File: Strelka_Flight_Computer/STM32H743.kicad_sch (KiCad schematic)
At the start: 45 parts, among them J3 Conn_01x07, Q3 AO3400A, Q4 AO3400A, Q5 AO3401A, SW2 TS-1185-C-A-A-A, SW3 TS-1185-C-A-A-A, U6 STM32H743VITx, Y1 Q13FC1350000400, Y2 X1E0000210834

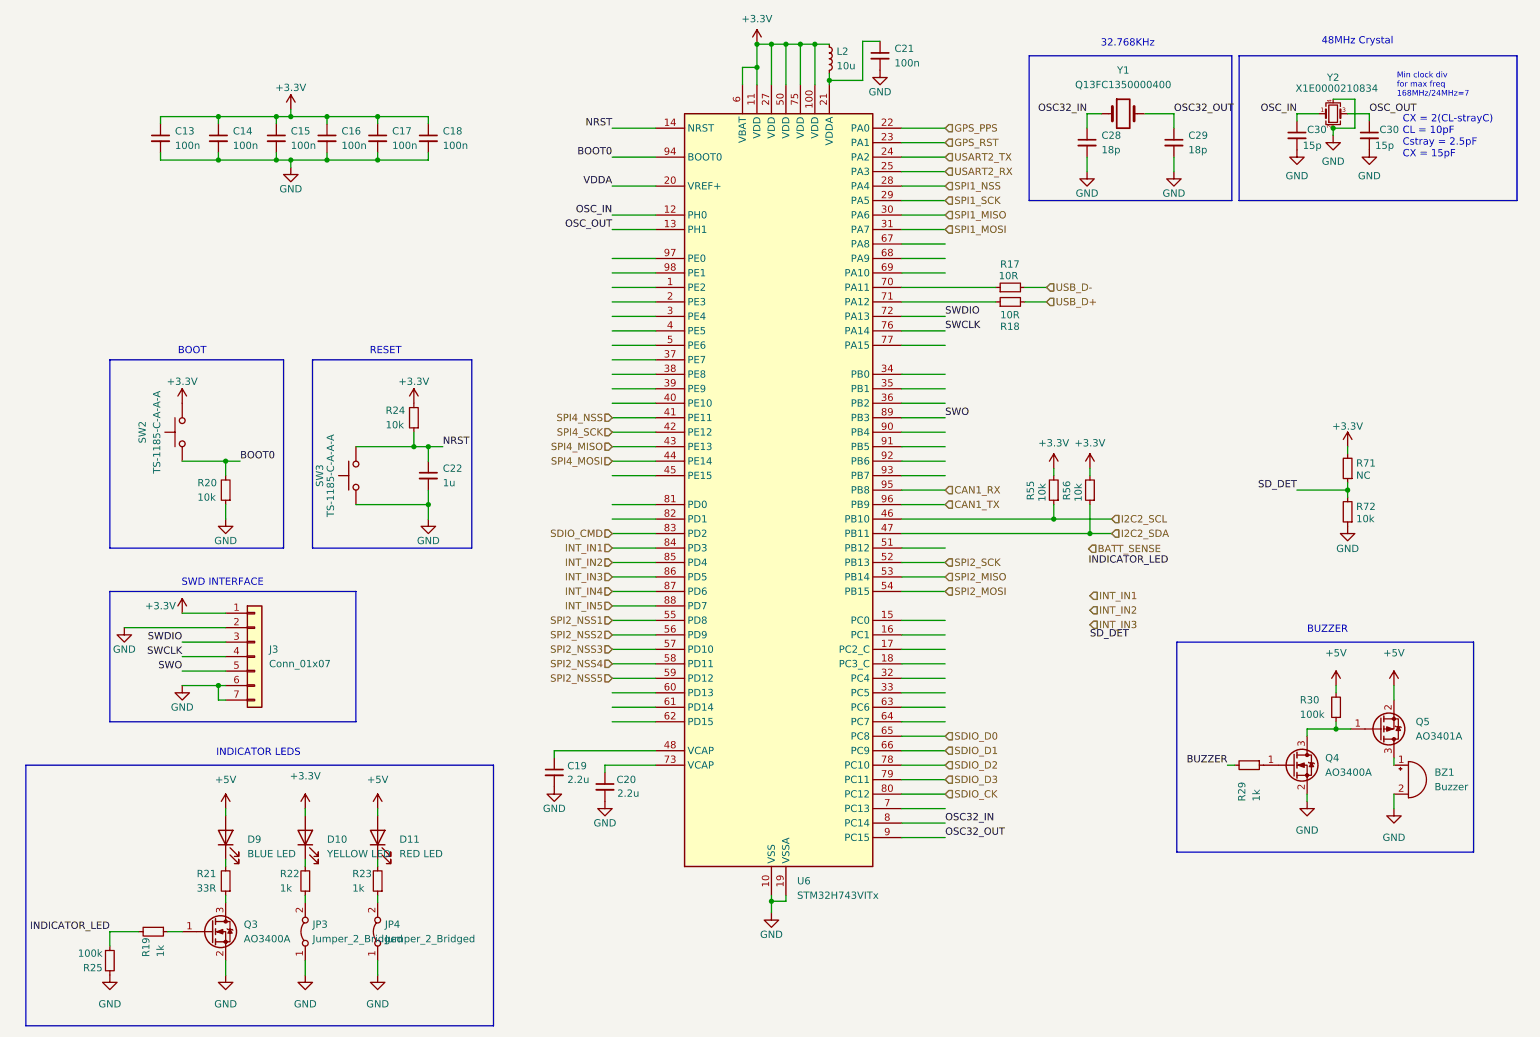
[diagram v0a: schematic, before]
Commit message: Started component placement
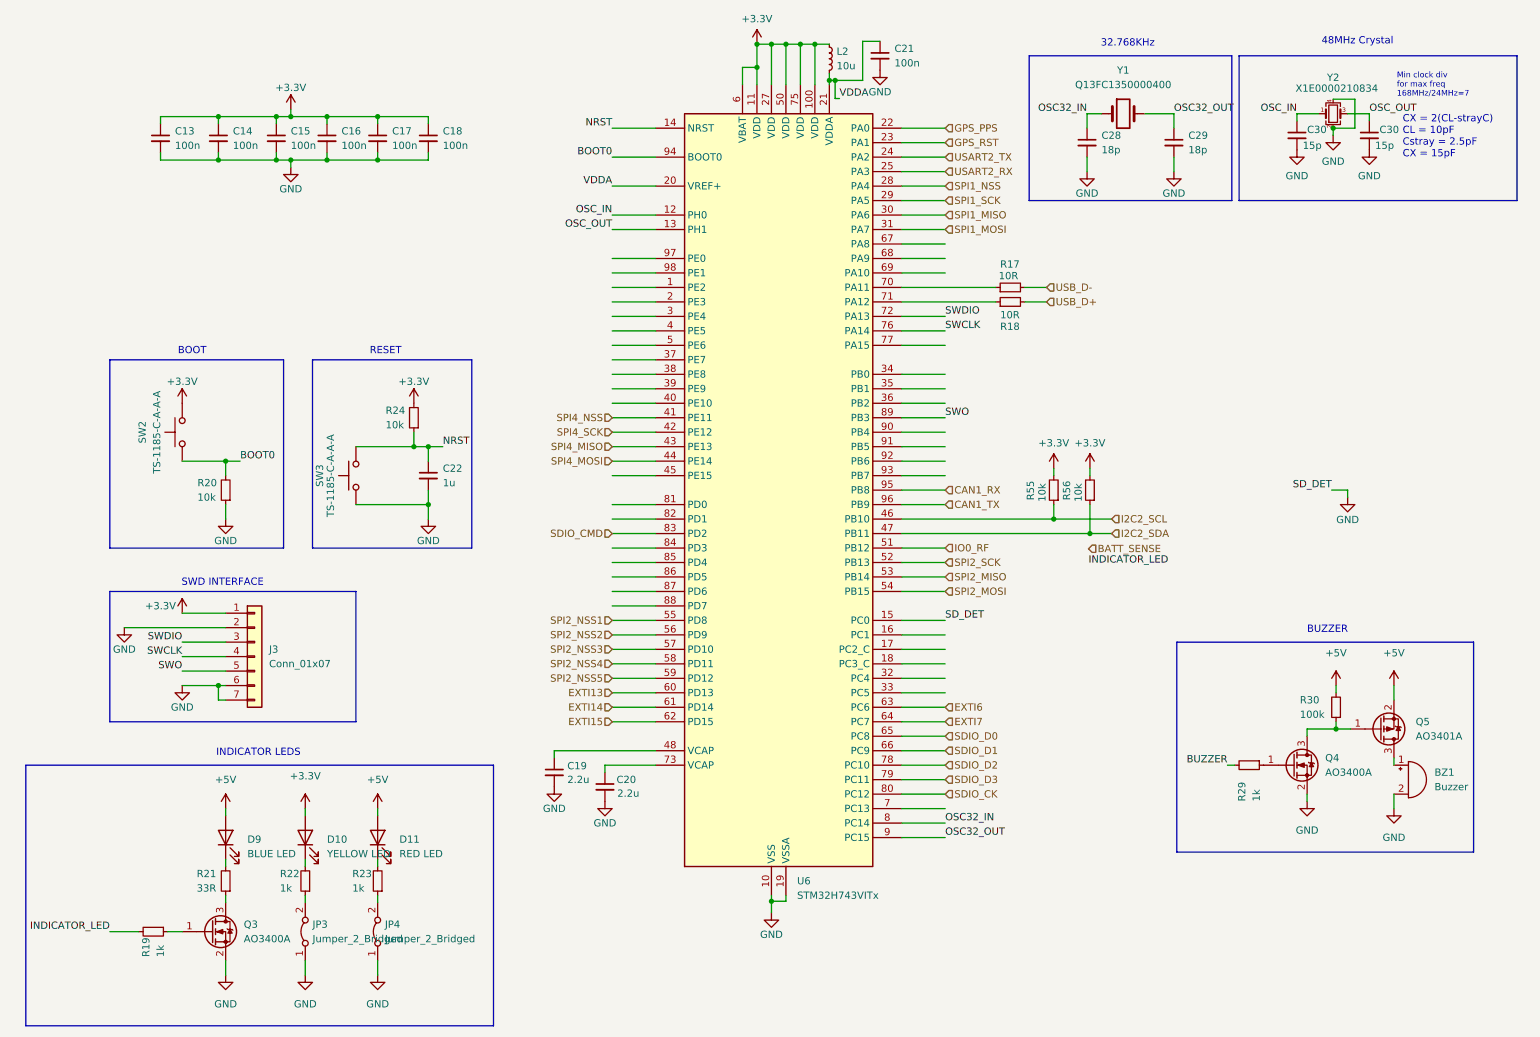
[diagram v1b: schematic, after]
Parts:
- removed R25: 100k, Resistor_SMD:R_0402_1005Metric, symbol Device:R_Small
- removed R71: NC, Resistor_SMD:R_0603_1608Metric_Pad0.98x0.95mm_HandSolder, symbol Device:R_Small
- removed R72: 10k, Resistor_SMD:R_0603_1608Metric_Pad0.98x0.95mm_HandSolder, symbol Device:R_Small
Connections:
- net GND: now also U6.15 (PC0)
- net VDDA: now also C21.1, L2.2, U6.21 (VDDA)
- net IO0_RF: now reaches U6.51 (PB12)
- net EXTI13: now reaches U6.60 (PD13)
- net EXTI14: now reaches U6.61 (PD14)
- net EXTI15: now reaches U6.62 (PD15)
- net EXTI6: now reaches U6.63 (PC6)
- net EXTI7: now reaches U6.64 (PC7)
- net INT_IN1: no longer names the net of U6.84 (PD3)
- net INT_IN2: no longer names the net of U6.85 (PD4)
- net INT_IN3: no longer names the net of U6.86 (PD5)
- net INT_IN4: no longer names the net of U6.87 (PD6)
- net INT_IN5: no longer names the net of U6.88 (PD7)

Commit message: Routing starting
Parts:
- removed R18: 10R, Resistor_SMD:R_0402_1005Metric, symbol Device:R_Small
- added R17: 10R, Resistor_SMD:R_0402_1005Metric, symbol Device:R_Small
- JP3, JP4: footprint Jumper:SolderJumper-2_P1.3mm_Bridged_Pad1.0x1.5mm -> Jumper:SolderJumper-2_P1.3mm_Bridged2Bar_RoundedPad1.0x1.5mm
- R17: LCSC (none) -> C25077
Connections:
- net USB_D+: now also R17.2
- net D-: now reaches R17.1, U6.70 (PA11)
- net D+: now reaches U6.71 (PA12)
- net D+: now also R17.1
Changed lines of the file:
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@@
     (effects (font (size 1.27 1.27)) (justify right bottom))
+  )
+  (label "D+" (at 185.674 62.992 0) (fields_autoplaced)
+    (effects (font (size 1.27 1.27)) (justify left bottom))
   )
   (label "SD_DET" (at 182.88 118.872 0) (fields_autoplaced)
@@
   )
   (label "OSC32_IN" (at 182.88 154.432 0) (fields_autoplaced)
+    (effects (font (size 1.27 1.27)) (justify left bottom))
+  )
+  (label "D-" (at 185.674 60.452 0) (fields_autoplaced)
     (effects (font (size 1.27 1.27)) (justify left bottom))
   )
@@
       (effects (font (size 1.27 1.27)) (justify right))
     )
-    (property "Footprint" "Jumper:SolderJumper-2_P1.3mm_Bridged_Pad1.0x1.5mm" (at 70.612 173.482 0)
+    (property "Footprint" "Jumper:SolderJumper-2_P1.3mm_Bridged2Bar_RoundedPad1.0x1.5mm" (at 70.612 173.482 0)
       (effects (font (size 1.27 1.27)) hide)
     )
@@
     )
     (property "Datasheet" "~" (at 194.31 60.452 0)
+      (effects (font (size 1.27 1.27)) hide)
+    )
+    (property "LCSC" "C25077" (at 194.31 60.452 90)
       (effects (font (size 1.27 1.27)) hide)
     )
@@
         (path "/e63e39d7-6ac0-4ffd-8aa3-1841a4541b55/35f7b859-8b4f-4308-9fbf-2678b353144a"
           (reference "C64") (unit 1)
+        )
+      )
+    )
+  )
+  (symbol (lib_id "Device:R_Small") (at 194.31 62.992 90) (unit 1)
+    (in_bom yes) (on_board yes) (dnp no)
+    (property "Reference" "R17" (at 192.405 66.929 90)
+      (effects (font (size 1.27 1.27)) (justify right))
+    )
+    (property "Value" "10R" (at 192.405 65.151 90)
+      (effects (font (size 1.27 1.27)) (justify right))
+    )
+    (property "Footprint" "Resistor_SMD:R_0402_1005Metric" (at 194.31 62.992 0)
+      (effects (font (size 1.27 1.27)) hide)
+    )
+    (property "Datasheet" "~" (at 194.31 62.992 0)
+      (effects (font (size 1.27 1.27)) hide)
+    )
+    (property "LCSC" "C25077" (at 194.31 62.992 90)
+      (effects (font (size 1.27 1.27)) hide)
+    )
+    (pin "1")
+    (pin "2")
+    (instances
+      (project "Strelka_Power_Board"
+        (path "/83158c8b-22ee-48c3-a78a-e95d14e6b912/fc5f30c0-eb37-4e12-adf2-96b06c9ae2b0"
+          (reference "R17") (unit 1)
+        )
+      )
+      (project "Strelka_Flight_Computer"
+        (path "/e63e39d7-6ac0-4ffd-8aa3-1841a4541b55/35f7b859-8b4f-4308-9fbf-2678b353144a"
+          (reference "R22") (unit 1)
         )
       )
@@
     )
   )
-  (symbol (lib_id "Device:R_Small") (at 194.31 62.992 90) (unit 1)
-    (in_bom yes) (on_board yes) (dnp no)
-    (property "Reference" "R18" (at 192.532 67.31 90)
-      (effects (font (size 1.27 1.27)) (justify right))
-    )
-    (property "Value" "10R" (at 192.532 65.278 90)
-      (effects (font (size 1.27 1.27)) (justify right))
-    )
-    (property "Footprint" "Resistor_SMD:R_0402_1005Metric" (at 194.31 62.992 0)
-      (effects (font (size 1.27 1.27)) hide)
-    )
-    (property "Datasheet" "~" (at 194.31 62.992 0)
-      (effects (font (size 1.27 1.27)) hide)
-    )
-    (pin "1")
-    (pin "2")
-    (instances
-      (project "Strelka_Power_Board"
-        (path "/83158c8b-22ee-48c3-a78a-e95d14e6b912/fc5f30c0-eb37-4e12-adf2-96b06c9ae2b0"
-          (reference "R18") (unit 1)
-        )
-      )
-      (project "Strelka_Flight_Computer"
-        (path "/e63e39d7-6ac0-4ffd-8aa3-1841a4541b55/35f7b859-8b4f-4308-9fbf-2678b353144a"
-          (reference "R85") (unit 1)
-        )
-      )
-    )
-  )
   (symbol (lib_id "Jumper:Jumper_2_Bridged") (at 83.312 173.482 90) (unit 1)
     (in_bom no) (on_board yes) (dnp no) (fields_autoplaced)
@@
       (effects (font (size 1.27 1.27)) (justify right))
     )
-    (property "Footprint" "Jumper:SolderJumper-2_P1.3mm_Bridged_Pad1.0x1.5mm" (at 83.312 173.482 0)
-      (effects (font (size 1.27 1.27)) hide)
-    )
+    (property "Footprint" "Jumper:SolderJumper-2_P1.3mm_Bridged2Bar_RoundedPad1.0x1.5mm" (at 83.312 173.482 0)
+      (effects (font (size 1.27 1.27)) hide)
+    )

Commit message: Routing complete
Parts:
- removed JP3, JP4: Jumper_2_Bridged, Jumper:SolderJumper-2_P1.3mm_Bridged2Bar_RoundedPad1.0x1.5mm, symbol Jumper:Jumper_2_Bridged
- D11: value RED LED -> BLUE LED; LCSC C2286 -> C72041
- D9: value BLUE LED -> RED LED; LCSC C72041 -> C2286
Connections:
- net GND: now also R22.1, R23.1
- net DROGUE_H: now reaches U6.90 (PB4)
- net DROGUE_L: now reaches U6.91 (PB5)
- net MAIN_H: now reaches U6.92 (PB6)
- net MAIN_L: now reaches U6.93 (PB7)
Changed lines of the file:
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@@
     (stroke (width 0) (type default))
   )
-  (wire (pts (xy 70.612 178.562) (xy 70.612 181.102))
+  (wire (pts (xy 70.612 167.132) (xy 70.612 181.102))
     (stroke (width 0) (type default))
   )
@@
     (stroke (width 0) (type default))
   )
-  (wire (pts (xy 83.312 178.562) (xy 83.312 181.102))
-    (stroke (width 0) (type default))
-  )
   (wire (pts (xy 92.202 38.1) (xy 83.312 38.1))
     (stroke (width 0) (type default))
@@
     (stroke (width 0) (type default))
   )
-  (wire (pts (xy 83.312 167.132) (xy 83.312 168.402))
+  (wire (pts (xy 83.312 167.132) (xy 83.312 181.102))
     (stroke (width 0) (type default))
   )
@@
   )
   (wire (pts (xy 55.372 30.48) (xy 65.532 30.48))
-    (stroke (width 0) (type default))
-  )
-  (wire (pts (xy 70.612 167.132) (xy 70.612 168.402))
     (stroke (width 0) (type default))
   )
@@
     (effects (font (size 1.27 1.27)) (justify right))
   )
+  (hierarchical_label "MAIN_H" (shape input) (at 182.88 90.932 0) (fields_autoplaced)
+    (effects (font (size 1.27 1.27)) (justify left))
+  )
   (hierarchical_label "SPI2_MISO" (shape input) (at 182.88 111.252 0) (fields_autoplaced)
     (effects (font (size 1.27 1.27)) (justify left))
@@
     (effects (font (size 1.27 1.27)) (justify right))
   )
+  (hierarchical_label "MAIN_L" (shape input) (at 182.88 93.472 0) (fields_autoplaced)
+    (effects (font (size 1.27 1.27)) (justify left))
+  )
   (hierarchical_label "USART2_TX" (shape input) (at 182.88 37.592 0) (fields_autoplaced)
     (effects (font (size 1.27 1.27)) (justify left))
@@
     (effects (font (size 1.27 1.27)) (justify right))
   )
+  (hierarchical_label "DROGUE_H" (shape input) (at 182.88 85.852 0) (fields_autoplaced)
+    (effects (font (size 1.27 1.27)) (justify left))
+  )
   (hierarchical_label "SPI4_SCK" (shape input) (at 124.46 85.852 180) (fields_autoplaced)
     (effects (font (size 1.27 1.27)) (justify right))
@@
     (effects (font (size 1.27 1.27)) (justify left))
   )
+  (hierarchical_label "DROGUE_L" (shape input) (at 182.88 88.392 0) (fields_autoplaced)
+    (effects (font (size 1.27 1.27)) (justify left))
+  )
   (hierarchical_label "SPI2_NSS3" (shape input) (at 124.46 123.952 180) (fields_autoplaced)
     (effects (font (size 1.27 1.27)) (justify right))
@@
       (effects (font (size 1.27 1.27)) (justify right))
     )
-    (property "Value" "RED LED" (at 87.122 159.8294 90)
+    (property "Value" "BLUE LED" (at 87.122 159.8294 90)
       (effects (font (size 1.27 1.27)) (justify right))
     )
@@
       (effects (font (size 1.27 1.27)) hide)
     )
-    (property "LCSC" "C2286" (at 83.312 156.972 90)
+    (property "LCSC" "C72041" (at 83.312 156.972 90)
+      (effects (font (size 1.27 1.27)) hide)
+    )
+    (property "Field5" "" (at 83.312 156.972 90)
       (effects (font (size 1.27 1.27)) hide)
     )
@@
     )
   )
-  (symbol (lib_id "Jumper:Jumper_2_Bridged") (at 70.612 173.482 90) (unit 1)
-    (in_bom no) (on_board yes) (dnp no) (fields_autoplaced)
-    (property "Reference" "JP3" (at 71.882 172.2119 90)
-      (effects (font (size 1.27 1.27)) (justify right))
-    )
-    (property "Value" "Jumper_2_Bridged" (at 71.882 174.7519 90)
-      (effects (font (size 1.27 1.27)) (justify right))
-    )
-    (property "Footprint" "Jumper:SolderJumper-2_P1.3mm_Bridged2Bar_RoundedPad1.0x1.5mm" (at 70.612 173.482 0)
-      (effects (font (size 1.27 1.27)) hide)
-    )
-    (property "Datasheet" "~" (at 70.612 173.482 0)
-      (effects (font (size 1.27 1.27)) hide)
-    )
-    (pin "1")
-    (pin "2")
-    (instances
-      (project "Strelka_Power_Board"
-        (path "/83158c8b-22ee-48c3-a78a-e95d14e6b912/fc5f30c0-eb37-4e12-adf2-96b06c9ae2b0"
-          (reference "JP3") (unit 1)
-        )
-      )
-      (project "Strelka_Flight_Computer"
-        (path "/e63e39d7-6ac0-4ffd-8aa3-1841a4541b55/35f7b859-8b4f-4308-9fbf-2678b353144a"
-          (reference "JP6") (unit 1)
-        )
-      )
-    )
-  )
   (symbol (lib_id "Switch:SW_Push") (at 49.022 85.852 90) (unit 1)
     (in_bom yes) (on_board yes) (dnp no)
@@
       (effects (font (size 1.27 1.27)) (justify right))
     )
-    (property "Value" "BLUE LED" (at 60.452 159.8294 90)
+    (property "Value" "RED LED" (at 60.452 159.8294 90)
       (effects (font (size 1.27 1.27)) (justify right))
     )
@@
       (effects (font (size 1.27 1.27)) hide)
     )
-    (property "LCSC" "C72041" (at 56.642 156.972 90)
+    (property "LCSC" "C2286" (at 56.642 156.972 90)
+      (effects (font (size 1.27 1.27)) hide)
+    )
+    (property "Field5" "" (at 56.642 156.972 90)
       (effects (font (size 1.27 1.27)) hide)
     )
@@
         )
       )
-    )
-  )
-  (symbol (lib_id "Jumper:Jumper_2_Bridged") (at 83.312 173.482 90) (unit 1)
-    (in_bom no) (on_board yes) (dnp no) (fields_autoplaced)
-    (property "Reference" "JP4" (at 84.582 172.2119 90)
-      (effects (font (size 1.27 1.27)) (justify right))
-    )
-    (property "Value" "Jumper_2_Bridged" (at 84.582 174.7519 90)
-      (effects (font (size 1.27 1.27)) (justify right))
-    )
-    (property "Footprint" "Jumper:SolderJumper-2_P1.3mm_Bridged2Bar_RoundedPad1.0x1.5mm" (at 83.312 173.482 0)
-      (effects (font (size 1.27 1.27)) hide)
-    )
-    (property "Datasheet" "~" (at 83.312 173.482 0)
-      (effects (font (size 1.27 1.27)) hide)
-    )
-    (pin "1")
-    (pin "2")
-    (instances
-      (project "Strelka_Power_Board"
-        (path "/83158c8b-22ee-48c3-a78a-e95d14e6b912/fc5f30c0-eb37-4e12-adf2-96b06c9ae2b0"
-          (reference "JP4") (unit 1)
-        )
-      )
-      (project "Strelka_Flight_Computer"
-        (path "/e63e39d7-6ac0-4ffd-8aa3-1841a4541b55/35f7b859-8b4f-4308-9fbf-2678b353144a"
-          (reference "JP7") (unit 1)
-        )
-      )

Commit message: Created BOM
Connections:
- net BATT_SENSE: now also U6.32 (PC4)
- net INDICATOR_LED: now also U6.18 (PC3_C)
- net DROGUE_CONT: now reaches U6.33 (PC5)
- net MAIN_CONT: now reaches U6.34 (PB0)
- net RESET_RF: now reaches U6.35 (PB1)
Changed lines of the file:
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@@
     (effects (font (size 1.27 1.27)) (justify right bottom))
   )
-  (label "INDICATOR_LED" (at 208.026 109.22 0) (fields_autoplaced)
+  (label "INDICATOR_LED" (at 182.88 126.492 0) (fields_autoplaced)
     (effects (font (size 1.27 1.27)) (justify left bottom))
   )
@@
   )
   (hierarchical_label "SPI1_NSS" (shape input) (at 182.88 42.672 0) (fields_autoplaced)
+    (effects (font (size 1.27 1.27)) (justify left))
+  )
+  (hierarchical_label "MAIN_CONT" (shape input) (at 182.88 75.692 0) (fields_autoplaced)
     (effects (font (size 1.27 1.27)) (justify left))
   )
@@
   )
   (hierarchical_label "IO0_RF" (shape input) (at 182.88 106.172 0) (fields_autoplaced)
+    (effects (font (size 1.27 1.27)) (justify left))
+  )
+  (hierarchical_label "DROGUE_CONT" (shape input) (at 182.88 131.572 0) (fields_autoplaced)
     (effects (font (size 1.27 1.27)) (justify left))
   )
@@
     (effects (font (size 1.27 1.27)) (justify left))
   )
-  (hierarchical_label "BATT_SENSE" (shape input) (at 208.026 106.299 0) (fields_autoplaced)
+  (hierarchical_label "BATT_SENSE" (shape input) (at 182.88 129.032 0) (fields_autoplaced)
     (effects (font (size 1.27 1.27)) (justify left))
   )
@@
     (effects (font (size 1.27 1.27)) (justify right))
   )
+  (hierarchical_label "RESET_RF" (shape input) (at 182.88 78.232 0) (fields_autoplaced)
+    (effects (font (size 1.27 1.27)) (justify left))
+  )
   (hierarchical_label "SPI2_SCK" (shape input) (at 182.88 108.712 0) (fields_autoplaced)
